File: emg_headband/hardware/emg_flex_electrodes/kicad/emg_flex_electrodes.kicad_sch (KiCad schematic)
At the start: 8 parts, among them J1 TO MAIN BOARD J6 (FH34SRJ-12S)

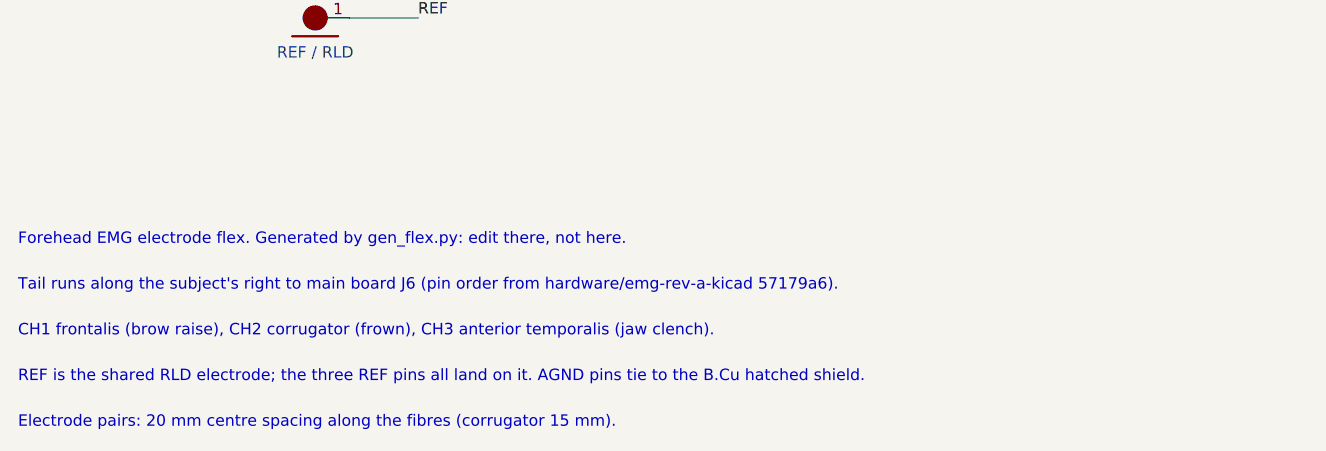
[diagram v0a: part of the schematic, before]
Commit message: Flex: 2.5 mm rivet holes and JLC fab outputs
Electrode holes are 2.7 mm for a DIN 660 2.5 mm copper rivet. Re-checked
J6 against main board c72bb90 (ESP32-S3 layout): same pins, still on the
right edge, so only the tail-length note changes. Adds gerbers, drill
and a PI stiffener layer for the FPC tab, plus JLC order settings in the
README. Electrode stiffener rings are dropped for rev 1.

Co-Authored-By: Claude Opus 5.5 (1M context) <noreply@anthropic.com>
Claude-Session: https://claude.ai/code/session_014gX5rSabikoFKBd7bBuHGf
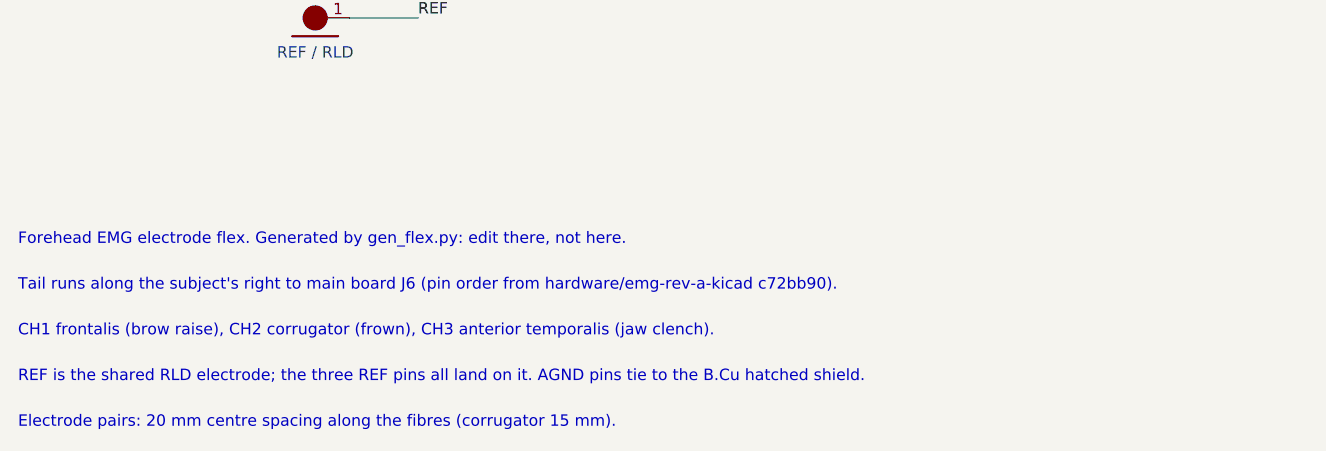
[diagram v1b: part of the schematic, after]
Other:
- note added: "Tail runs along the subject's right to main board J6 (pin order from hardware/emg-rev-a-kicad c72bb90)."
- note removed: "Tail runs along the subject's right to main board J6 (pin order from hardware/emg-rev-a-kicad 57179a6)."
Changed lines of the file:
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@@
   (label "REF" (at 165.10 102.87 180) (effects (font (size 1.27 1.27)) (justify right bottom)))
   (text "Forehead EMG electrode flex. Generated by gen_flex.py: edit there, not here." (at 30.48 152.40 0) (effects (font (size 1.27 1.27)) (justify left bottom)))
-  (text "Tail runs along the subject's right to main board J6 (pin order from hardware/emg-rev-a-kicad 57179a6)." (at 30.48 157.48 0) (effects (font (size 1.27 1.27)) (justify left bottom)))
+  (text "Tail runs along the subject's right to main board J6 (pin order from hardware/emg-rev-a-kicad c72bb90)." (at 30.48 157.48 0) (effects (font (size 1.27 1.27)) (justify left bottom)))
   (text "CH1 frontalis (brow raise), CH2 corrugator (frown), CH3 anterior temporalis (jaw clench)." (at 30.48 162.56 0) (effects (font (size 1.27 1.27)) (justify left bottom)))
   (text "REF is the shared RLD electrode; the three REF pins all land on it. AGND pins tie to the B.Cu hatched shield." (at 30.48 167.64 0) (effects (font (size 1.27 1.27)) (justify left bottom)))

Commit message: Flex: tie the shield to REF, leave AGND pins open
Each signal trace has ~35-55 pF to the hatched shield. On AGND that adds
to the main board's 100 pF input caps and costs dry-electrode CMRR; at
REF (RLD-driven body potential) it carries no common mode. AGND guard
lanes are removed so P and N see the same neighbours. Copper width and
thickness checked: <4 ohm per trace, noise negligible. Gerbers updated.

Co-Authored-By: Claude Opus 5.5 (1M context) <noreply@anthropic.com>
Claude-Session: https://claude.ai/code/session_014gX5rSabikoFKBd7bBuHGf
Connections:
- removed net AGND: J1.1 (AGND), J1.5 (AGND), J1.9 (AGND)
- no-connect marks 0 -> 3
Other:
- note added: "REF is the shared RLD electrode; the three REF pins all land on it. Main board AGND pins 1/5/9 are not connected; the B.Cu hatched shield is tied to REF."
- note removed: "REF is the shared RLD electrode; the three REF pins all land on it. AGND pins tie to the B.Cu hatched shield."
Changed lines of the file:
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@@
     (instances (project "emg_flex_electrodes" (path "/6f8c0656-9087-5cf8-af87-9101f5d1b6df" (reference "J1") (unit 1))))
   )
-  (wire (pts (xy 172.72 74.93) (xy 165.10 74.93)) (stroke (width 0) (type default)))
-  (label "AGND" (at 165.10 74.93 180) (effects (font (size 1.27 1.27)) (justify right bottom)))
+  (no_connect (at 172.72 74.93))
   (wire (pts (xy 172.72 77.47) (xy 165.10 77.47)) (stroke (width 0) (type default)))
   (label "CH1P" (at 165.10 77.47 180) (effects (font (size 1.27 1.27)) (justify right bottom)))
@@
   (wire (pts (xy 172.72 82.55) (xy 165.10 82.55)) (stroke (width 0) (type default)))
   (label "REF" (at 165.10 82.55 180) (effects (font (size 1.27 1.27)) (justify right bottom)))
-  (wire (pts (xy 172.72 85.09) (xy 165.10 85.09)) (stroke (width 0) (type default)))
-  (label "AGND" (at 165.10 85.09 180) (effects (font (size 1.27 1.27)) (justify right bottom)))
+  (no_connect (at 172.72 85.09))
   (wire (pts (xy 172.72 87.63) (xy 165.10 87.63)) (stroke (width 0) (type default)))
   (label "CH2P" (at 165.10 87.63 180) (effects (font (size 1.27 1.27)) (justify right bottom)))
@@
   (wire (pts (xy 172.72 92.71) (xy 165.10 92.71)) (stroke (width 0) (type default)))
   (label "REF" (at 165.10 92.71 180) (effects (font (size 1.27 1.27)) (justify right bottom)))
-  (wire (pts (xy 172.72 95.25) (xy 165.10 95.25)) (stroke (width 0) (type default)))
-  (label "AGND" (at 165.10 95.25 180) (effects (font (size 1.27 1.27)) (justify right bottom)))
+  (no_connect (at 172.72 95.25))
   (wire (pts (xy 172.72 97.79) (xy 165.10 97.79)) (stroke (width 0) (type default)))
   (label "CH3P" (at 165.10 97.79 180) (effects (font (size 1.27 1.27)) (justify right bottom)))
@@
   (text "Tail runs along the subject's right to main board J6 (pin order from hardware/emg-rev-a-kicad c72bb90)." (at 30.48 157.48 0) (effects (font (size 1.27 1.27)) (justify left bottom)))
   (text "CH1 frontalis (brow raise), CH2 corrugator (frown), CH3 anterior temporalis (jaw clench)." (at 30.48 162.56 0) (effects (font (size 1.27 1.27)) (justify left bottom)))
-  (text "REF is the shared RLD electrode; the three REF pins all land on it. AGND pins tie to the B.Cu hatched shield." (at 30.48 167.64 0) (effects (font (size 1.27 1.27)) (justify left bottom)))
+  (text "REF is the shared RLD electrode; the three REF pins all land on it. Main board AGND pins 1/5/9 are not connected; the B.Cu hatched shield is tied to REF." (at 30.48 167.64 0) (effects (font (size 1.27 1.27)) (justify left bottom)))
   (text "Electrode pairs: 20 mm centre spacing along the fibres (corrugator 15 mm)." (at 30.48 172.72 0) (effects (font (size 1.27 1.27)) (justify left bottom)))
   (sheet_instances (path "/" (page "1")))
